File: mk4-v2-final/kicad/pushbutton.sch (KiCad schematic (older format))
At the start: 1 part

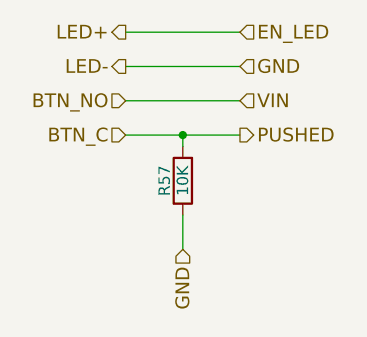
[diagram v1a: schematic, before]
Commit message: added headnight diodes, I don't think software control of them is going to be possible
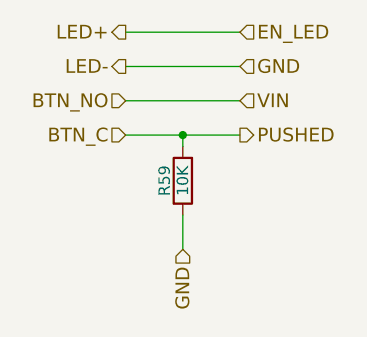
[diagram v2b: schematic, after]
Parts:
- renumbered R52 to R46
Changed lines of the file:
@@
 	5600 3350 6100 3350
 $Comp
-L R R52
+L R R46
 U 1 1 5A1C999A
 P 5850 3700
-AR Path="/59DEA30F/5A1C69FD/5A1C999A" Ref="R52"  Part="1"
-AR Path="/59DEA30F/5A1D83EB/5A1C999A" Ref="R53"  Part="1"
-AR Path="/59DEA30F/5A1D9BE8/5A1C999A" Ref="R54"  Part="1"
-AR Path="/59DEA30F/5A1E0E34/5A1C999A" Ref="R55"  Part="1"
-AR Path="/59DEA30F/5A1E0E62/5A1C999A" Ref="R56"  Part="1"
-AR Path="/59DEA30F/5A1E2C27/5A1C999A" Ref="R57"  Part="1"
-AR Path="/59DEA30F/5A1E2C55/5A1C999A" Ref="R58"  Part="1"
-AR Path="/59DEA30F/5A1E2C83/5A1C999A" Ref="R59"  Part="1"
-AR Path="/59DEA30F/5A1E2D0D/5A1C999A" Ref="R60"  Part="1"
-AR Path="/59DEA30F/5A1E92C0/5A1C999A" Ref="R61"  Part="1"
-AR Path="/59DEA30F/5A1E92EE/5A1C999A" Ref="R62"  Part="1"
-AR Path="/59DEA30F/5A1E931C/5A1C999A" Ref="R63"  Part="1"
-AR Path="/59DEA30F/5A1E934A/5A1C999A" Ref="R64"  Part="1"
-AR Path="/59DEA30F/5A1E9378/5A1C999A" Ref="R65"  Part="1"
-AR Path="/59DEA30F/5A1E93A6/5A1C999A" Ref="R66"  Part="1"
-F 0 "R57" V 5930 3700 50  0000 C CNN
+AR Path="/59DEA30F/5A1C69FD/5A1C999A" Ref="R46"  Part="1"
+AR Path="/59DEA30F/5A1D83EB/5A1C999A" Ref="R47"  Part="1"
+AR Path="/59DEA30F/5A1E0E34/5A1C999A" Ref="R48"  Part="1"
+AR Path="/59DEA30F/5A1E0E62/5A1C999A" Ref="R49"  Part="1"
+AR Path="/59DEA30F/5A1E2C27/5A1C999A" Ref="R50"  Part="1"
+AR Path="/59DEA30F/5A1E2C55/5A1C999A" Ref="R51"  Part="1"
+AR Path="/59DEA30F/5A1E2C83/5A1C999A" Ref="R52"  Part="1"
+AR Path="/59DEA30F/5A1E2D0D/5A1C999A" Ref="R53"  Part="1"
+AR Path="/59DEA30F/5A1E92C0/5A1C999A" Ref="R54"  Part="1"
+AR Path="/59DEA30F/5A1E92EE/5A1C999A" Ref="R55"  Part="1"
+AR Path="/59DEA30F/5A1E931C/5A1C999A" Ref="R56"  Part="1"
+AR Path="/59DEA30F/5A1E934A/5A1C999A" Ref="R57"  Part="1"
+AR Path="/59DEA30F/5A1E9378/5A1C999A" Ref="R58"  Part="1"
+AR Path="/59DEA30F/5A1E93A6/5A1C999A" Ref="R59"  Part="1"
+F 0 "R59" V 5930 3700 50  0000 C CNN
 F 1 "10K" V 5850 3700 50  0000 C CNN
 F 2 "Resistors_THT:R_Axial_DIN0207_L6.3mm_D2.5mm_P10.16mm_Horizontal" V 5780 3700 50  0001 C CNN

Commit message: schematic is done, footprint association and netlist are also done
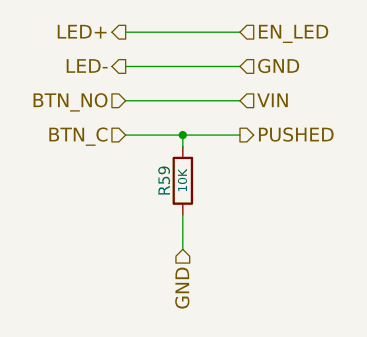
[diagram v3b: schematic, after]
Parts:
- R46: footprint Resistors_THT:R_Axial_DIN0207_L6.3mm_D2.5mm_P10.16mm_Horizontal -> Resistors_THT:R_Axial_DIN0204_L3.6mm_D1.6mm_P5.08mm_Horizontal; digikey-pn (none) -> BC10.0KXCT-ND; mfg-pn (none) -> MBA02040C1002FRP00
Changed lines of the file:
@@
 EESchema Schematic File Version 2
-LIBS:hitchco-mk4-rescue
 LIBS:power
 LIBS:device
@@
 LIBS:cd4013b
 LIBS:ncs3s1205sc
+LIBS:lca715
+LIBS:SN74HC595N
+LIBS:CD74HC4067
 LIBS:hitchco-mk4-cache
 EELAYER 25 0
@@
 $Descr A4 11693 8268
 encoding utf-8
-Sheet 35 54
+Sheet 18 54
 Title ""
 Date ""
@@
 Comment4 ""
 $EndDescr
-Text HLabel 5600 3050 0    60   Output ~ 0
-LED+
-Text HLabel 5600 3350 0    60   Input ~ 0
-BTN_NO
-Text HLabel 5600 3500 0    60   Input ~ 0
-BTN_C
-Text HLabel 6100 3350 2    60   Input ~ 0
-VIN
-Wire Wire Line
-	5600 3350 6100 3350
 $Comp
 L R R46
@@
 AR Path="/59DEA30F/5A1E93A6/5A1C999A" Ref="R59"  Part="1"
 F 0 "R59" V 5930 3700 50  0000 C CNN
-F 1 "10K" V 5850 3700 50  0000 C CNN
-F 2 "Resistors_THT:R_Axial_DIN0207_L6.3mm_D2.5mm_P10.16mm_Horizontal" V 5780 3700 50  0001 C CNN
+F 1 "10K" V 5850 3700 39  0000 C CNN
+F 2 "Resistors_THT:R_Axial_DIN0204_L3.6mm_D1.6mm_P5.08mm_Horizontal" V 5780 3700 50  0001 C CNN
 F 3 "" H 5850 3700 50  0001 C CNN
+F 4 "BC10.0KXCT-ND" H 5930 3800 50  0001 C CNN "digikey-pn"
+F 5 "MBA02040C1002FRP00" H 5930 3800 50  0001 C CNN "mfg-pn"
 	1    5850 3700
 	-1   0    0    1
 $EndComp
+Text HLabel 5600 3050 0    60   Output ~ 0
+LED+
+Text HLabel 5600 3350 0    60   Input ~ 0
+BTN_NO
+Text HLabel 5600 3500 0    60   Input ~ 0
+BTN_C
+Text HLabel 6100 3350 2    60   Input ~ 0
+VIN
+Text HLabel 6100 3500 2    60   Output ~ 0
+PUSHED
+Text HLabel 5850 4000 3    60   Input ~ 0
+GND
+Text HLabel 6100 3050 2    60   Input ~ 0
+EN_LED
+Text HLabel 5600 3200 0    60   Output ~ 0
+LED-
+Text HLabel 6100 3200 2    60   Input ~ 0
+GND
+Wire Wire Line
+	5600 3350 6100 3350
 Wire Wire Line
 	5600 3500 6100 3500
 Wire Wire Line
 	5850 3500 5850 3550
-Text HLabel 6100 3500 2    60   Output ~ 0
-PUSHED
-Connection ~ 5850 3500
-Text HLabel 5850 4000 3    60   Input ~ 0
-GND
 Wire Wire Line
 	5850 4000 5850 3850
-Text HLabel 6100 3050 2    60   Input ~ 0
-EN_LED
-Text HLabel 5600 3200 0    60   Output ~ 0
-LED-
 Wire Wire Line
 	6100 3050 5600 3050
-Text HLabel 6100 3200 2    60   Input ~ 0
-GND
 Wire Wire Line
 	6100 3200 5600 3200
+Connection ~ 5850 3500
 $EndSCHEMATC

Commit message: all components on the board
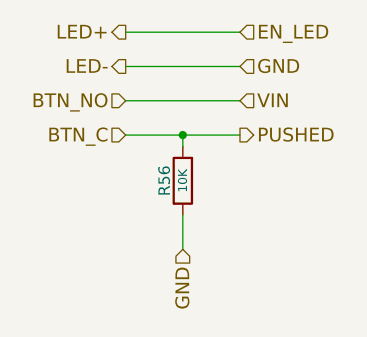
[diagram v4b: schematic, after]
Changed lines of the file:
@@
 AR Path="/59DEA30F/5A1E9378/5A1C999A" Ref="R58"  Part="1"
 AR Path="/59DEA30F/5A1E93A6/5A1C999A" Ref="R59"  Part="1"
-F 0 "R59" V 5930 3700 50  0000 C CNN
+F 0 "R56" V 5930 3700 50  0000 C CNN
 F 1 "10K" V 5850 3700 39  0000 C CNN
 F 2 "Resistors_THT:R_Axial_DIN0204_L3.6mm_D1.6mm_P5.08mm_Horizontal" V 5780 3700 50  0001 C CNN

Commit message: all files are in, time to order!
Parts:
- R46: value 10K -> 10KΩ
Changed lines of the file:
@@
 AR Path="/59DEA30F/5A1E9378/5A1C999A" Ref="R58"  Part="1"
 AR Path="/59DEA30F/5A1E93A6/5A1C999A" Ref="R59"  Part="1"
-F 0 "R56" V 5930 3700 50  0000 C CNN
-F 1 "10K" V 5850 3700 39  0000 C CNN
+F 0 "R46" V 5930 3700 50  0000 C CNN
+F 1 "10KΩ" V 5850 3700 39  0000 C CNN
 F 2 "Resistors_THT:R_Axial_DIN0204_L3.6mm_D1.6mm_P5.08mm_Horizontal" V 5780 3700 50  0001 C CNN
 F 3 "" H 5850 3700 50  0001 C CNN
